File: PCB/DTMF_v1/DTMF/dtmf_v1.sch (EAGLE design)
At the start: 37 parts, among them IC1 ATTINY84A-SSF, IC2 MT8870DS1, Q1 MCQ4406A-TP, Q2 MCQ4406A-TP, Y1 ATS080B-E, Y2 ATS080B-E

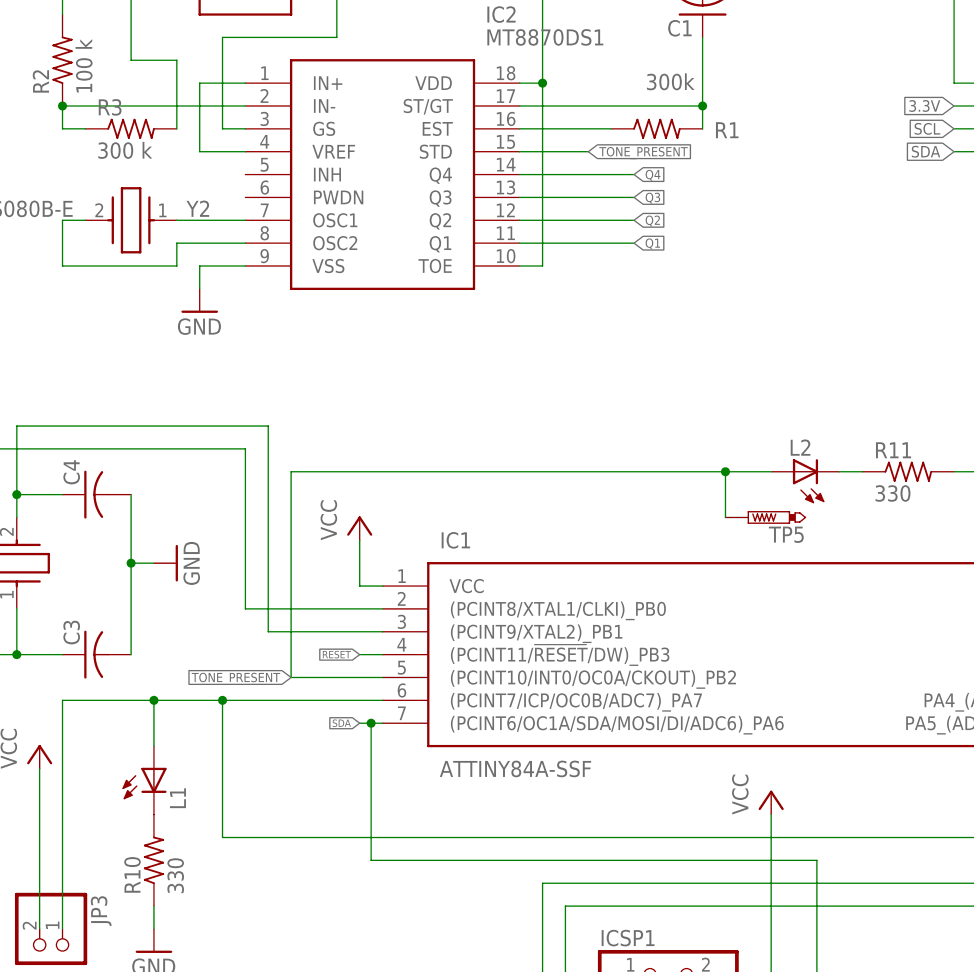
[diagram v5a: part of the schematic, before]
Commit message: added openhw log,slot for internal leds
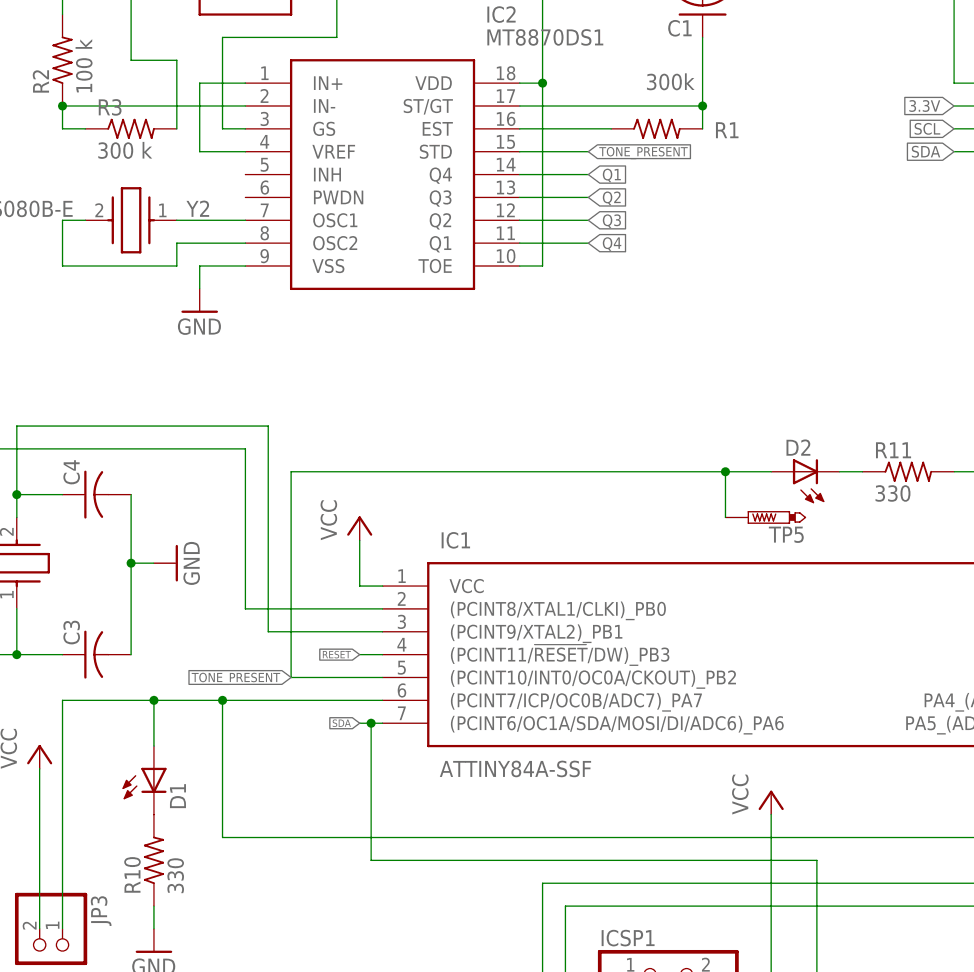
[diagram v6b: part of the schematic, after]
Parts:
- renumbered L1 to D1, L2 to D2
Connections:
- net Q1: now also IC2.Q4; no longer IC2.Q1
- net Q2: now also IC2.Q3; no longer IC2.Q2
- net Q3: now also IC2.Q2; no longer IC2.Q3
- net Q4: now also IC2.Q1; no longer IC2.Q4
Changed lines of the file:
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@@
 <setting verticaltext="up"/>
 </settings>
-<grid distance="0.05" unitdist="inch" unit="inch" style="lines" multiple="1" display="yes" altdistance="0.01" altunitdist="inch" altunit="inch"/>
+<grid distance="0.1" unitdist="inch" unit="inch" style="lines" multiple="1" display="no" altdistance="0.01" altunitdist="inch" altunit="inch"/>
 <layers>
 <layer number="1" name="Top" color="4" fill="1" visible="no" active="no"/>
@@
 <part name="GND5" library="supply1" library_urn="urn:adsk.eagle:library:371" deviceset="GND" device=""/>
 <part name="P+4" library="supply1" library_urn="urn:adsk.eagle:library:371" deviceset="VCC" device=""/>
-<part name="L1" library="adafruit" deviceset="LED" device="CHIP-LED0805"/>
+<part name="D1" library="adafruit" deviceset="LED" device="CHIP-LED0805"/>
 <part name="GND6" library="supply1" library_urn="urn:adsk.eagle:library:371" deviceset="GND" device=""/>
 <part name="R10" library="rcl" library_urn="urn:adsk.eagle:library:334" deviceset="R-US_" device="M0805" package3d_urn="urn:adsk.eagle:package:23556/2" value="330"/>
@@
 <part name="GND7" library="supply1" library_urn="urn:adsk.eagle:library:371" deviceset="GND" device=""/>
 <part name="ICSP1" library="pinhead" library_urn="urn:adsk.eagle:library:325" deviceset="PINHD-2X3" device="" package3d_urn="urn:adsk.eagle:package:22462/2"/>
-<part name="L2" library="adafruit" deviceset="LED" device="CHIP-LED0805"/>
+<part name="D2" library="adafruit" deviceset="LED" device="CHIP-LED0805"/>
 <part name="R11" library="rcl" library_urn="urn:adsk.eagle:library:334" deviceset="R-US_" device="M0805" package3d_urn="urn:adsk.eagle:package:23556/2" value="330"/>
 <part name="GND8" library="supply1" library_urn="urn:adsk.eagle:library:371" deviceset="GND" device=""/>
@@
 <attribute name="VALUE" x="7.62" y="50.8" size="1.778" layer="96" rot="R90"/>
 </instance>
-<instance part="L1" gate="G$1" x="22.86" y="50.8" smashed="yes">
+<instance part="D1" gate="G$1" x="22.86" y="50.8" smashed="yes">
 <attribute name="NAME" x="26.416" y="46.228" size="1.778" layer="95" rot="R90"/>
 <attribute name="VALUE" x="28.575" y="46.228" size="1.778" layer="96" rot="R90"/>
@@
 <attribute name="VALUE" x="72.39" y="17.78" size="1.778" layer="96"/>
 </instance>
-<instance part="L2" gate="G$1" x="93.98" y="83.82" smashed="yes" rot="R90">
+<instance part="D2" gate="G$1" x="93.98" y="83.82" smashed="yes" rot="R90">
 <attribute name="NAME" x="96.012" y="87.376" size="1.778" layer="95" rot="R180"/>
 <attribute name="VALUE" x="98.552" y="89.535" size="1.778" layer="96" rot="R180"/>
@@
 <wire x1="38.1" y1="60.96" x2="38.1" y2="83.82" width="0.1524" layer="91"/>
 <wire x1="38.1" y1="83.82" x2="86.36" y2="83.82" width="0.1524" layer="91"/>
-<pinref part="L2" gate="G$1" pin="A"/>
+<pinref part="D2" gate="G$1" pin="A"/>
 <wire x1="86.36" y1="83.82" x2="91.44" y2="83.82" width="0.1524" layer="91"/>
 <junction x="86.36" y="83.82"/>
@@
 </segment>
 <segment>
-<pinref part="IC2" gate="G$1" pin="Q4"/>
-<wire x1="76.2" y1="116.84" x2="63.5" y2="116.84" width="0.1524" layer="91"/>
-<label x="76.2" y="116.84" size="1.016" layer="95" xref="yes"/>
+<pinref part="IC2" gate="G$1" pin="Q1"/>
+<wire x1="63.5" y1="109.22" x2="71.12" y2="109.22" width="0.1524" layer="91"/>
+<label x="71.12" y="109.22" size="1.27" layer="95" xref="yes"/>
 </segment>
 </net>
@@
 </segment>
 <segment>
-<pinref part="IC2" gate="G$1" pin="Q2"/>
-<wire x1="63.5" y1="111.76" x2="76.2" y2="111.76" width="0.1524" layer="91"/>
-<label x="76.2" y="111.76" size="1.016" layer="95" xref="yes"/>
+<pinref part="IC2" gate="G$1" pin="Q3"/>
+<wire x1="63.5" y1="114.3" x2="71.12" y2="114.3" width="0.1524" layer="91"/>
+<label x="71.12" y="114.3" size="1.27" layer="95" xref="yes"/>
 </segment>
 </net>
@@
 <pinref part="JP2" gate="A" pin="3"/>
 <wire x1="147.32" y1="30.48" x2="165.1" y2="30.48" width="0.1524" layer="91"/>
-<pinref part="L1" gate="G$1" pin="A"/>
+<pinref part="D1" gate="G$1" pin="A"/>
 <wire x1="22.86" y1="53.34" x2="22.86" y2="58.42" width="0.1524" layer="91"/>
 <junction x="22.86" y="58.42"/>
@@
 <net name="N$23" class="0">
 <segment>
-<pinref part="L1" gate="G$1" pin="C"/>
+<pinref part="D1" gate="G$1" pin="C"/>
 <pinref part="R10" gate="G$1" pin="2"/>
 </segment>
@@
 <net name="N$25" class="0">
 <segment>
-<pinref part="L2" gate="G$1" pin="C"/>
+<pinref part="D2" gate="G$1" pin="C"/>
 <pinref part="R11" gate="G$1" pin="1"/>
 <wire x1="99.06" y1="83.82" x2="101.6" y2="83.82" width="0.1524" layer="91"/>
@@
 </segment>
 <segment>
-<pinref part="IC2" gate="G$1" pin="Q1"/>
-<wire x1="63.5" y1="109.22" x2="76.2" y2="109.22" width="0.1524" layer="91"/>
-<label x="76.2" y="109.22" size="1.016" layer="95" xref="yes"/>
+<pinref part="IC2" gate="G$1" pin="Q4"/>
+<wire x1="63.5" y1="116.84" x2="71.12" y2="116.84" width="0.1524" layer="91"/>
+<label x="71.12" y="116.84" size="1.27" layer="95" xref="yes"/>
 </segment>
 </net>
@@
 </segment>
 <segment>
-<pinref part="IC2" gate="G$1" pin="Q3"/>
-<wire x1="63.5" y1="114.3" x2="76.2" y2="114.3" width="0.1524" layer="91"/>
-<label x="76.2" y="114.3" size="1.016" layer="95" xref="yes"/>
-</segment>
-</net>
+<pinref part="IC2" gate="G$1" pin="Q2"/>
+<wire x1="63.5" y1="111.76" x2="71.12" y2="111.76" width="0.1524" layer="91"/>
+<label x="71.12" y="111.76" size="1.27" layer="95" xref="yes"/>
+</segment>
+</net>

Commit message: final board design
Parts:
- renumbered ICSP1 to ICSP
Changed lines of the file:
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@@
 <part name="P+5" library="supply1" library_urn="urn:adsk.eagle:library:371" deviceset="VCC" device=""/>
 <part name="GND7" library="supply1" library_urn="urn:adsk.eagle:library:371" deviceset="GND" device=""/>
-<part name="ICSP1" library="pinhead" library_urn="urn:adsk.eagle:library:325" deviceset="PINHD-2X3" device="" package3d_urn="urn:adsk.eagle:package:22462/2"/>
+<part name="ICSP" library="pinhead" library_urn="urn:adsk.eagle:library:325" deviceset="PINHD-2X3" device="" package3d_urn="urn:adsk.eagle:package:22462/2"/>
 <part name="D2" library="adafruit" deviceset="LED" device="CHIP-LED0805"/>
 <part name="R11" library="rcl" library_urn="urn:adsk.eagle:library:334" deviceset="R-US_" device="M0805" package3d_urn="urn:adsk.eagle:package:23556/2" value="330"/>
@@
 <attribute name="VALUE" x="86.36" y="15.24" size="1.778" layer="96"/>
 </instance>
-<instance part="ICSP1" gate="A" x="78.74" y="25.4" smashed="yes">
+<instance part="ICSP" gate="A" x="78.74" y="25.4" smashed="yes">
 <attribute name="NAME" x="72.39" y="31.115" size="1.778" layer="95"/>
 <attribute name="VALUE" x="72.39" y="17.78" size="1.778" layer="96"/>
@@
 <junction x="152.4" y="58.42"/>
 <wire x1="152.4" y1="38.1" x2="66.04" y2="38.1" width="0.1524" layer="91"/>
-<pinref part="ICSP1" gate="A" pin="3"/>
+<pinref part="ICSP" gate="A" pin="3"/>
 <wire x1="66.04" y1="38.1" x2="66.04" y2="25.4" width="0.1524" layer="91"/>
 <wire x1="66.04" y1="25.4" x2="76.2" y2="25.4" width="0.1524" layer="91"/>
@@
 <segment>
 <wire x1="46.99" y1="40.64" x2="96.52" y2="40.64" width="0.1524" layer="91"/>
-<pinref part="ICSP1" gate="A" pin="4"/>
+<pinref part="ICSP" gate="A" pin="4"/>
 <wire x1="83.82" y1="25.4" x2="96.52" y2="25.4" width="0.1524" layer="91"/>
 <wire x1="96.52" y1="25.4" x2="96.52" y2="40.64" width="0.1524" layer="91"/>
@@
 </segment>
 <segment>
-<pinref part="ICSP1" gate="A" pin="6"/>
+<pinref part="ICSP" gate="A" pin="6"/>
 <wire x1="83.82" y1="22.86" x2="88.9" y2="22.86" width="0.1524" layer="91"/>
 <pinref part="GND7" gate="1" pin="GND"/>
@@
 </segment>
 <segment>
-<pinref part="ICSP1" gate="A" pin="2"/>
+<pinref part="ICSP" gate="A" pin="2"/>
 <wire x1="83.82" y1="27.94" x2="91.44" y2="27.94" width="0.1524" layer="91"/>
 <pinref part="P+5" gate="VCC" pin="VCC"/>
@@
 </segment>
 <segment>
-<pinref part="ICSP1" gate="A" pin="5"/>
+<pinref part="ICSP" gate="A" pin="5"/>
 <wire x1="76.2" y1="22.86" x2="68.58" y2="22.86" width="0.1524" layer="91"/>
 <label x="68.58" y="22.86" size="0.8128" layer="95" rot="R180" xref="yes"/>
@@
 <wire x1="149.86" y1="35.56" x2="68.58" y2="35.56" width="0.1524" layer="91"/>
 <wire x1="68.58" y1="35.56" x2="68.58" y2="27.94" width="0.1524" layer="91"/>
-<pinref part="ICSP1" gate="A" pin="1"/>
+<pinref part="ICSP" gate="A" pin="1"/>
 <wire x1="68.58" y1="27.94" x2="76.2" y2="27.94" width="0.1524" layer="91"/>
 <pinref part="JP2" gate="A" pin="1"/>
